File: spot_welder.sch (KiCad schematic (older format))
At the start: 20 parts, among them J1 Conn_01x02_Female, J2 Conn_01x02_Female, Q1 BSR20, Q2 BSR20, Q3 BSR20, SW1 Rotary_Encoder_Switch, U1 Stm8S103F6_module, U2 KCSA02-123, U3 KCSA02-123, U4 KCSA02-123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

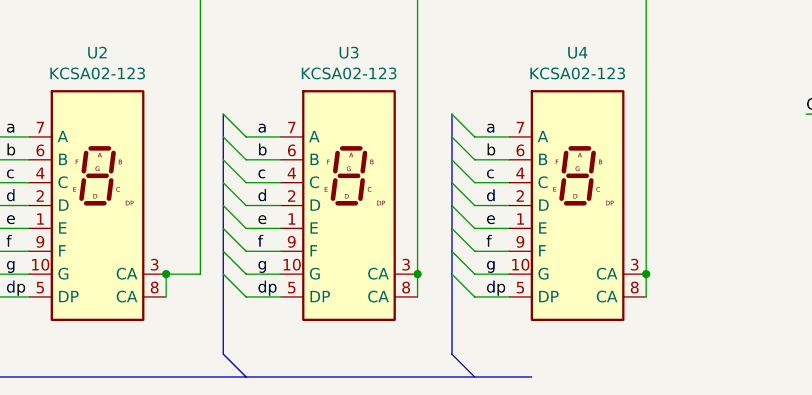
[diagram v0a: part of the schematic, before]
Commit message: stm8 module footprint changed
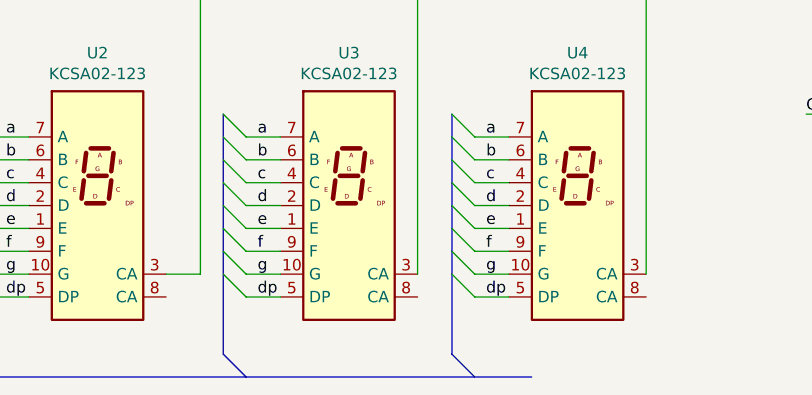
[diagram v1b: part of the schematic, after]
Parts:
- U1: footprint Package_DIP:DIP-20_W7.62mm -> ebay_modules:DIP-20_600_ELL
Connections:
- net at Q1.2 (E), U2.3 (CA): no longer U2.8 (CA)
- net at Q2.2 (E), U3.3 (CA): no longer U3.8 (CA)
- net at Q3.2 (E), U4.3 (CA): no longer U4.8 (CA)
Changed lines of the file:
@@
 F 0 "U1" H 1650 2968 50  0000 C CNN
 F 1 "Stm8S103F6_module" H 1650 2877 50  0000 C CNN
-F 2 "Package_DIP:DIP-20_W7.62mm" H 1450 2450 50  0001 C CNN
+F 2 "ebay_modules:DIP-20_600_ELL" H 1450 2450 50  0001 C CNN
 F 3 "" H 1450 2450 50  0001 C CNN
 	1    1350 2700
@@
 $EndComp
 Wire Wire Line
-	5400 4800 5400 4700
-Wire Wire Line
 	4400 2500 4400 4700
-Connection ~ 4400 4700
-Wire Wire Line
-	4400 4700 4400 4800
-Wire Wire Line
-	3300 4800 3300 4700
-Connection ~ 3300 4700
 Connection ~ 3450 2100
 Wire Wire Line
@@
 Wire Wire Line
 	5400 2500 5400 4700
-Connection ~ 5400 4700
 Wire Wire Line
 	4950 2500 5400 2500
@@
 Wire Wire Line
 	3450 4700 3300 4700
-$Comp
-L Display_Character:KCSA02-123 U2
-U 1 1 5EED545F
-P 3000 4400
-F 0 "U2" H 3000 5067 50  0000 C CNN
-F 1 "KCSA02-123" H 3000 4976 50  0000 C CNN
-F 2 "Display_7Segment:7SegmentLED_LTS6760_LTS6780" H 3000 3800 50  0001 C CNN
-F 3 "http://www.kingbright.com/attachments/file/psearch/000/00/00/KCSA02-123(Ver.9A).pdf" H 2500 4875 50  0001 L CNN
-	1    3000 4400
-	1    0    0    -1
-$EndComp
 Wire Wire Line
 	3450 4700 3450 2500
@@
 Wire Bus Line
 	2450 2600 2450 5050
+$Comp
+L Display_Character:KCSA02-123 U2
+U 1 1 5EED545F
+P 3000 4400
+F 0 "U2" H 3000 5067 50  0000 C CNN
+F 1 "KCSA02-123" H 3000 4976 50  0000 C CNN
+F 2 "Display_7Segment:7SegmentLED_LTS6760_LTS6780" H 3000 3800 50  0001 C CNN
+F 3 "http://www.kingbright.com/attachments/file/psearch/000/00/00/KCSA02-123(Ver.9A).pdf" H 2500 4875 50  0001 L CNN
+	1    3000 4400
+	1    0    0    -1
+$EndComp
 $EndSCHEMATC

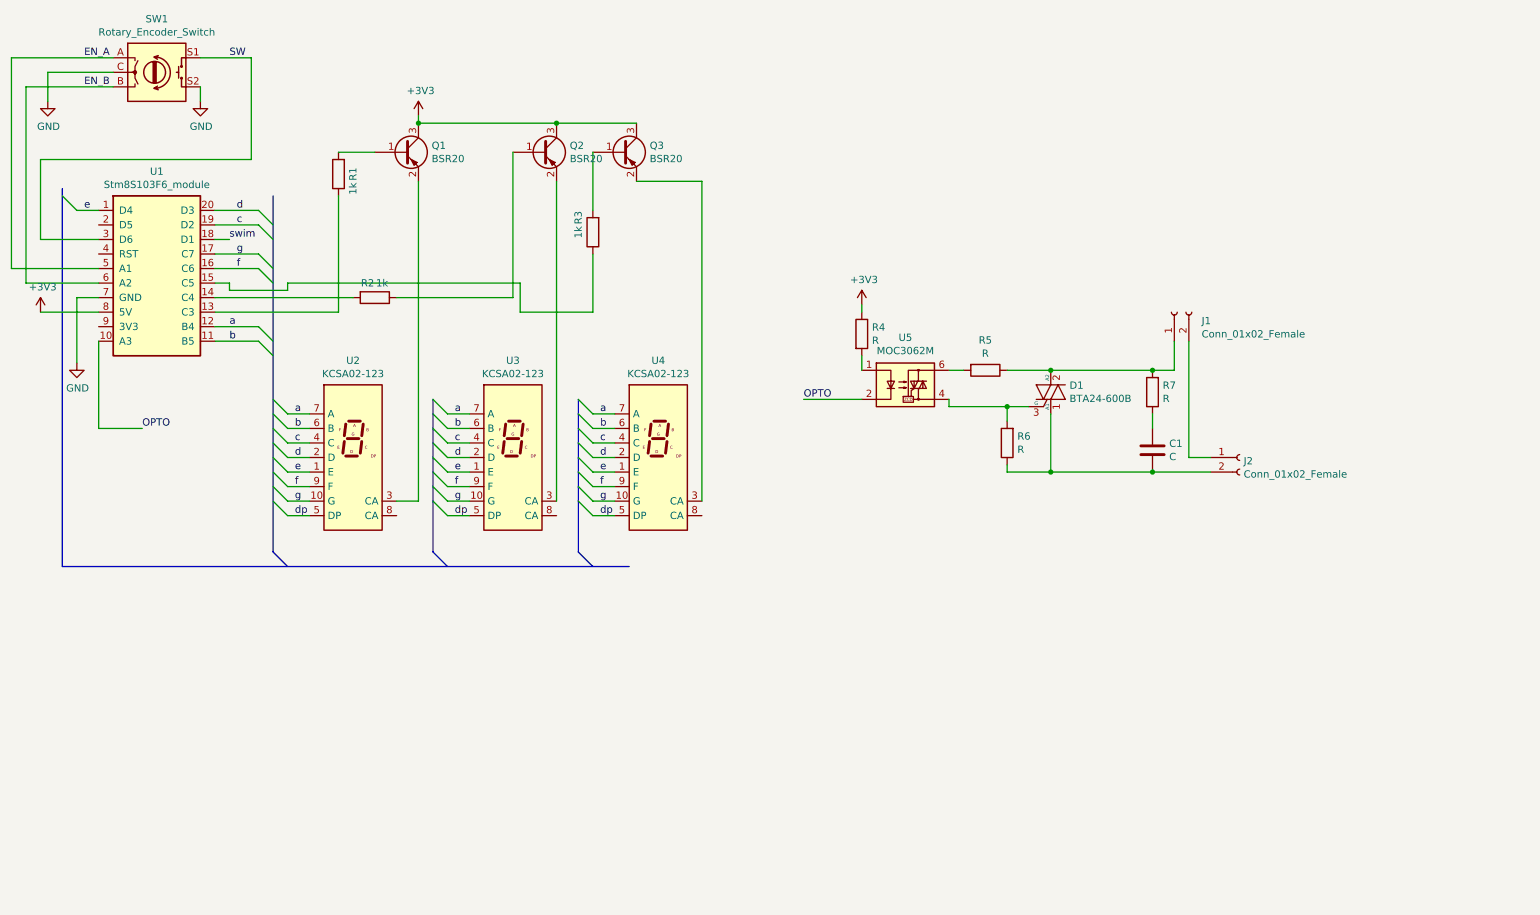
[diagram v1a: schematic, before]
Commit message: mounting holes added
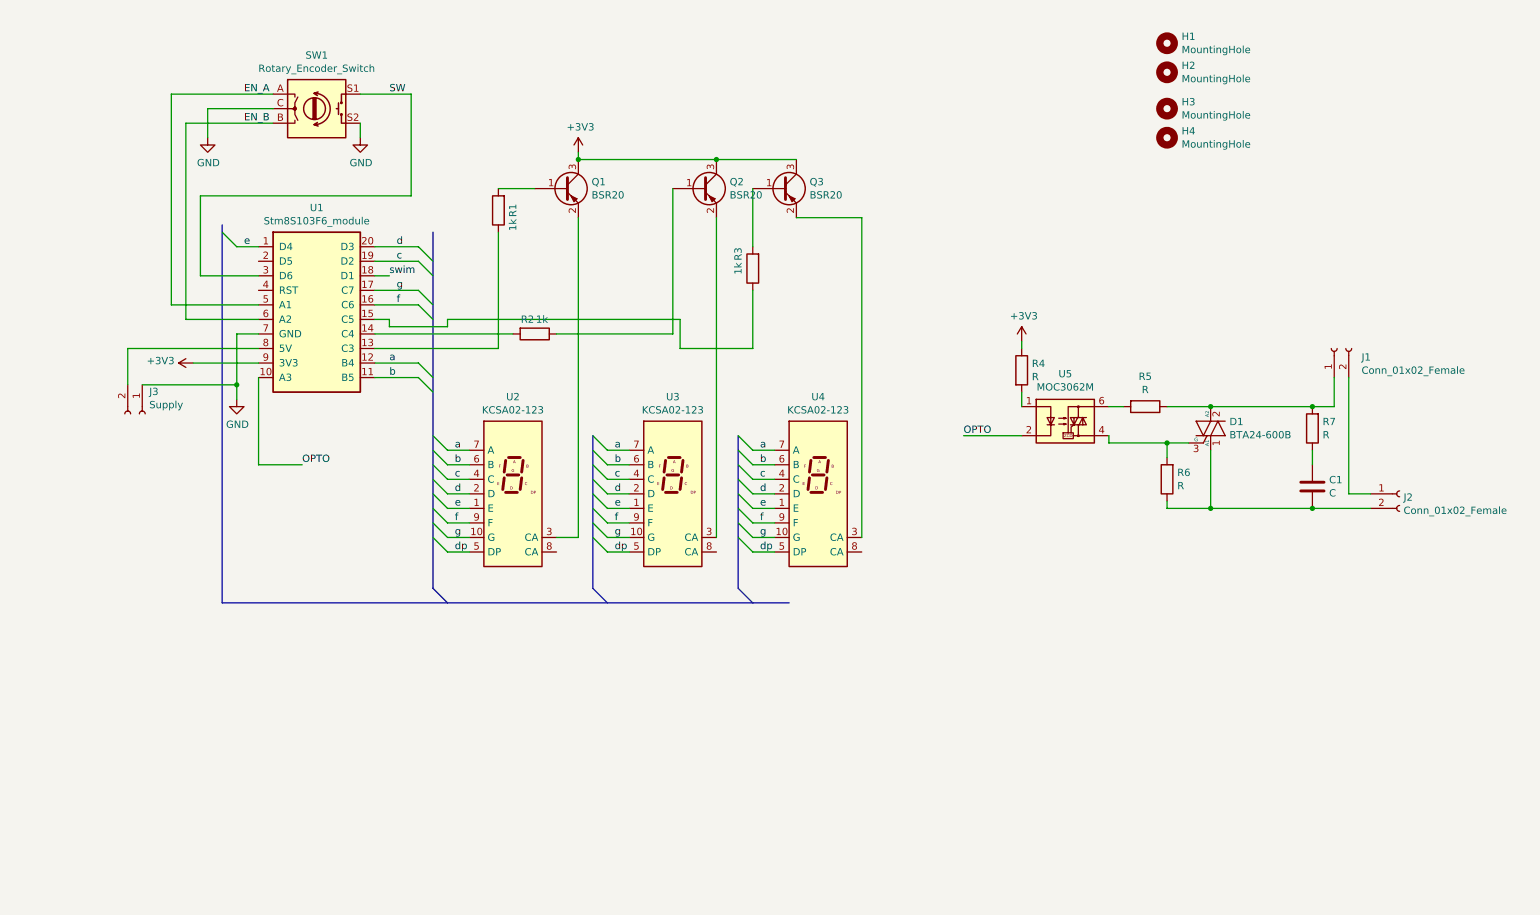
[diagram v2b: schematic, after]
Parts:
- added H1, H2, H3, H4: MountingHole, MountingHole:MountingHole_3.2mm_M3_DIN965_Pad, symbol Mechanical:MountingHole
- added J3: Supply, Connector_Phoenix_GMSTB:PhoenixContact_GMSTBVA_2,5_2-G-7,62_1x02_P7.62mm_Vertical, symbol Connector:Conn_01x02_Female
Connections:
- net +3V3: now also U1.9 (3V3); no longer U1.8 (5V)
- net GND: now also J3.1 (Pin_1)
- new net: J3.2 (Pin_2), U1.8 (5V)
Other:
- moved on the sheet: C1, D1, J1, J2, Q1, Q2, Q3, R1, R2, R3, R4, R5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

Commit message: Add segment resistors
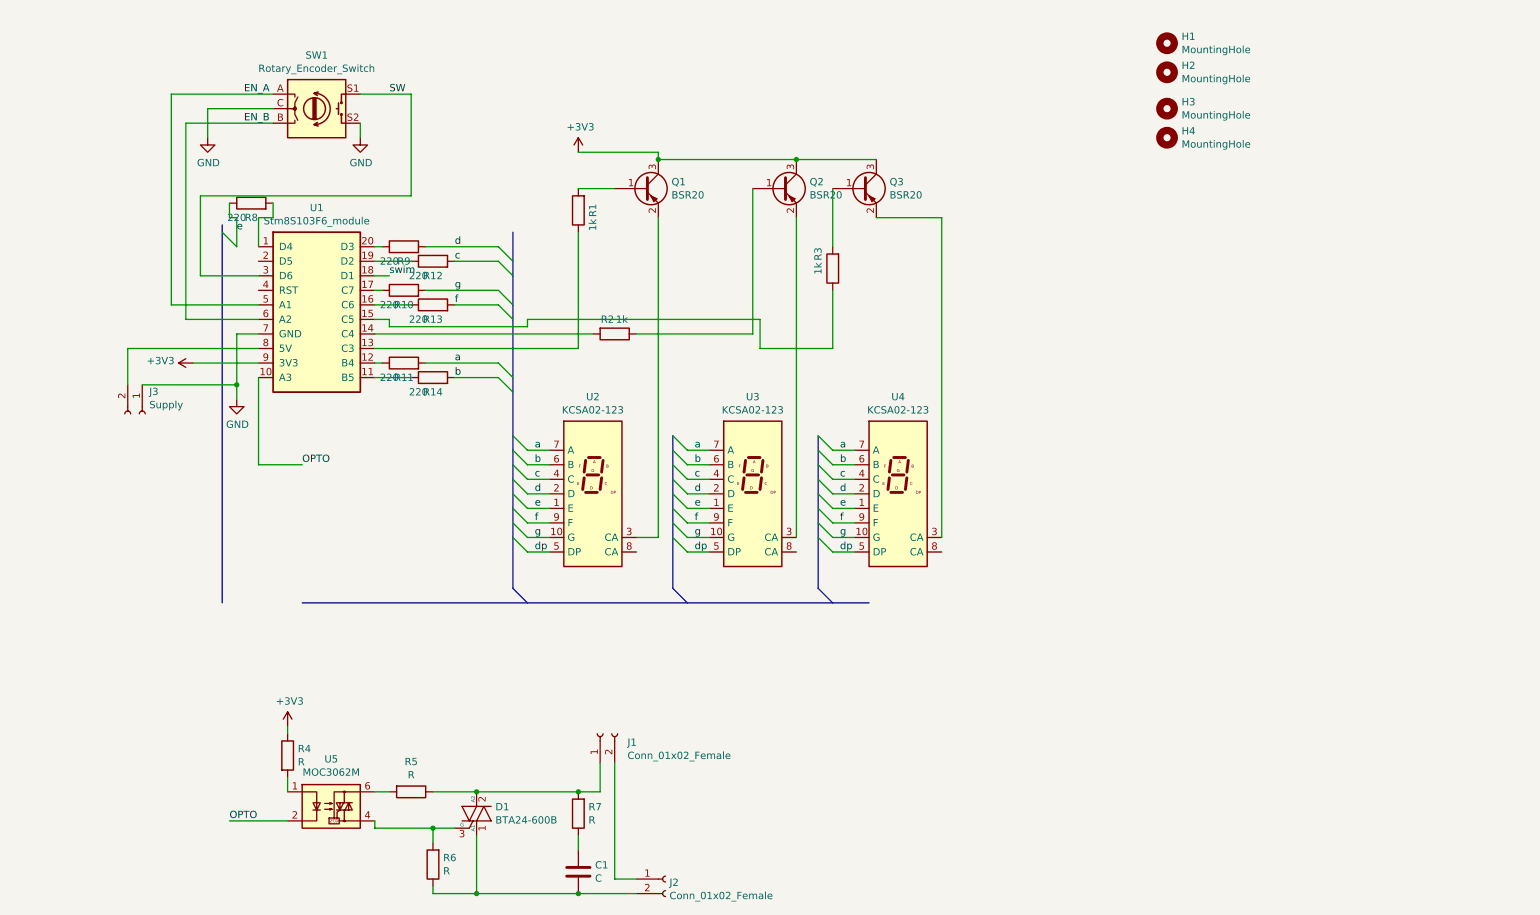
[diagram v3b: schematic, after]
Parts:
- added R10, R11, R12, R13, R14, R8, R9: 220, Resistor_SMD:R_0805_2012Metric_Pad1.15x1.40mm_HandSolder, symbol Device:R
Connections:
- net a: now also R11.2; no longer U1.12 (B4)
- net b: now also R14.2; no longer U1.11 (B5)
- net c: now also R12.2; no longer U1.19 (D2)
- net d: now also R9.2; no longer U1.20 (D3)
- net e: now also R8.1; no longer U1.1 (D4)
- net f: now also R13.2; no longer U1.16 (C6)
- net g: now also R10.2; no longer U1.17 (C7)
- new net: R8.2, U1.1 (D4)
- new net: R14.1, U1.11 (B5)
- new net: R11.1, U1.12 (B4)
- new net: R13.1, U1.16 (C6)
- new net: R10.1, U1.17 (C7)
- new net: R12.1, U1.19 (D2)
- new net: R9.1, U1.20 (D3)
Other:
- moved on the sheet: C1, D1, J1, J2, Q1, Q2, Q3, R1, R2, R3, R4, R5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

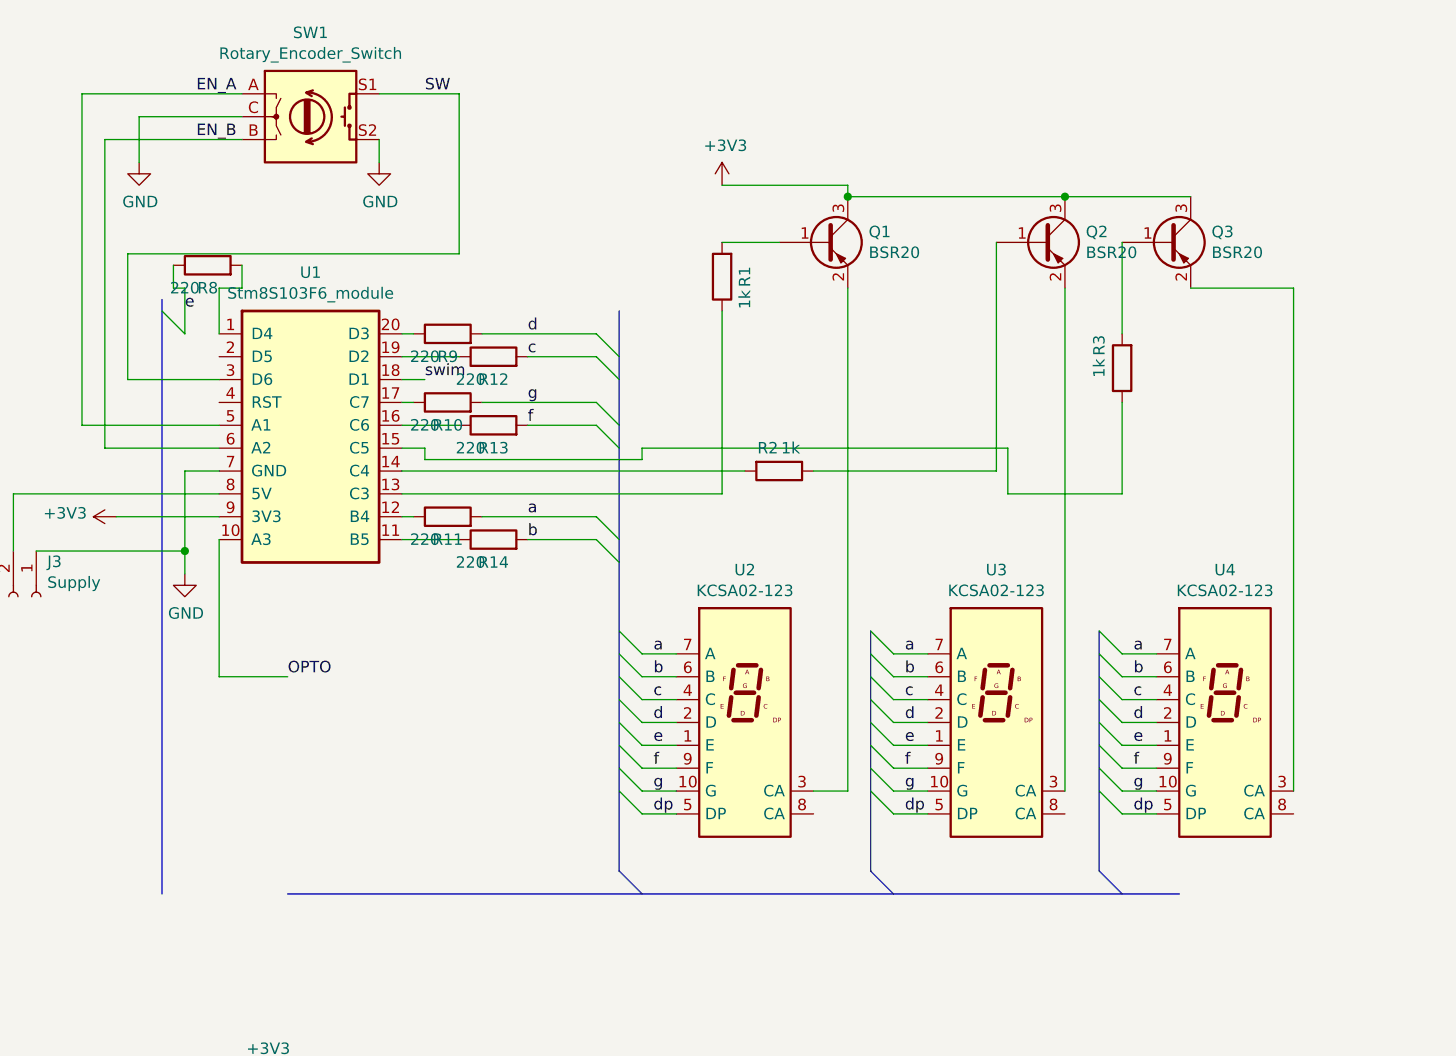
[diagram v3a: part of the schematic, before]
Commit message: 3x7seg LED module
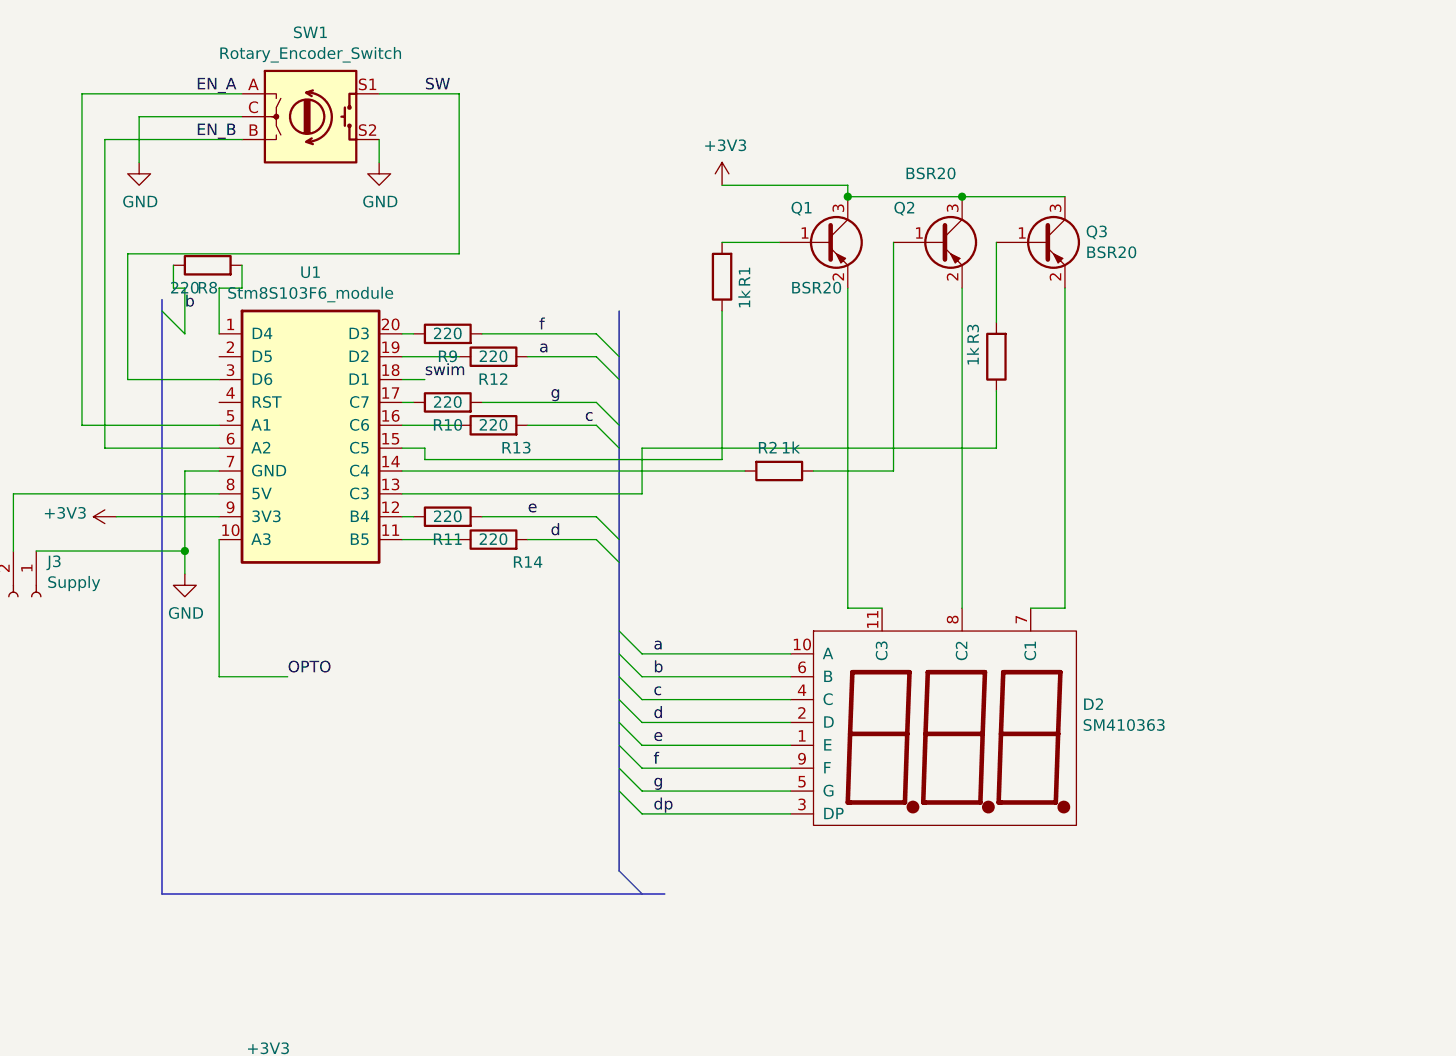
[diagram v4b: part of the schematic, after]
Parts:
- removed U2, U3, U4: KCSA02-123, Display_7Segment:7SegmentLED_LTS6760_LTS6780, symbol Display_Character:KCSA02-123
- added D2: SM410363, ebay_modules:SM410363, symbol marcin_schematic:SM410363
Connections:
- net a: now also R12.2, D2.10 (A); no longer R11.2
- net b: now also R8.1, D2.6 (B); no longer R14.2
- net c: now also R13.2, D2.4 (C); no longer R12.2
- net d: now also R14.2, D2.2 (D); no longer R9.2
- net dp: now also D2.3 (DP)
- net e: now also R11.2, D2.1 (E); no longer R8.1
- net f: now also R9.2, D2.9 (F); no longer R13.2
- net g: now also D2.5 (G)
- net at U1.13 (C3): now also R3.1; no longer R1.1
- net at U1.15 (C5): now also R1.1; no longer R3.1
- net at Q1.2 (E): now also D2.11 (C3)
- net at Q2.2 (E): now also D2.8 (C2)
- net at Q3.2 (E): now also D2.7 (C1)
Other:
- moved on the sheet: Q2, Q3, R3
